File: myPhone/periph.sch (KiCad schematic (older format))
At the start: 57 parts, among them J201 ESP32.UART, J202 Modem, J203 SIM_Card, J204 Motor, J205 Micro_SD_Card, J206 Camera, J207 GPS, SW201 BOOT, U201 ESP32-WROOM, U202 SN74CBTLV3125, U203 TXB0104RGY, U204 TXB0104RGY, U205 DRV2605L, U206 SN74CBTLV3126, U207 TPS22917, U208 SN74LVC2G66, U209 TPS22917

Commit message: upgrade to kicad 5; fixed footprints
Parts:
- removed J201: ESP32.UART, Pin_Headers:Pin_Header_Straight_1x03_Pitch2.54mm, symbol Conn_01x03
- removed J202: Modem, footprints:mpcie-socket, symbol Conn_02x26_Odd_Even
- removed J203: SIM_Card, footprints:Wurth_NanoSIM-693043020611, symbol SIM_Card
- removed J204: Motor, Pin_Headers:Pin_Header_Straight_1x02_Pitch1.27mm, symbol Conn_01x02
- removed J205: Micro_SD_Card, footprints:MicroSd, symbol Micro_SD_Card
- removed J206: Camera, Pin_Headers:Pin_Header_Straight_1x08_Pitch2.54mm, symbol Conn_01x08
- removed J207: GPS, Pin_Headers:Pin_Header_Straight_1x04_Pitch2.54mm, symbol Conn_01x04
- removed JP202: UART SW, Pin_Headers:Pin_Header_Straight_2x04_Pitch1.27mm, symbol Conn_02x04_Odd_Even
- removed SW201: BOOT, footprints:Panasonic_EVPBB, symbol SW_Push
- removed U203, U204: TXB0104RGY, footprints:Texas_S-PVQFN-N14_ThermalVias, symbol TXB0104RGY
- added J201: ESP32.UART, Connector_PinHeader_2.54mm:PinHeader_1x03_P2.54mm_Vertical, symbol Connector_Generic:Conn_01x03
- added J202: Modem, footprints:mpcie-socket, symbol Connector_Generic:Conn_02x26_Odd_Even
- added J203: SIM_Card, footprints:Wurth_NanoSIM-693043020611, symbol Connector:SIM_Card
- added J204: Motor, Connector_PinHeader_1.27mm:PinHeader_1x02_P1.27mm_Vertical, symbol Connector_Generic:Conn_01x02
- added J205: Micro_SD_Card, footprints:MicroSd, symbol Connector:Micro_SD_Card
- added J206: Camera, Connector_PinHeader_2.54mm:PinHeader_1x08_P2.54mm_Vertical, symbol Connector_Generic:Conn_01x08
- added J207: GPS, Connector_PinHeader_2.54mm:PinHeader_1x04_P2.54mm_Vertical, symbol Connector_Generic:Conn_01x04
- added JP202: UART SW, Connector_PinHeader_1.27mm:PinHeader_2x04_P1.27mm_Vertical, symbol Connector_Generic:Conn_02x04_Odd_Even
- added SW201: BOOT, footprints:Panasonic_EVPBB, symbol Switch:SW_Push
- added U203, U204: TXB0104RGY, Package_DFN_QFN:Texas_S-PVQFN-N14_ThermalVias, symbol Logic_LevelTranslator:TXB0104RGY
- C201, C202, C203, C204, C205, C206, C207, C208, C210, C211, C212, C213, C214, C215, C216, C217, C218, C219, C220, C221, C222, C223, C224, C225, C226: footprint Capacitors_SMD:C_0603 -> Capacitor_SMD:C_0603_1608Metric; symbol C -> Device:C
- C209: footprint Capacitors_Tantalum_SMD:CP_Tantalum_Case-B_EIA-3528-21_Reflow -> Capacitor_Tantalum_SMD:CP_EIA-3528-21_Kemet-B; symbol CP -> Device:CP
- JP201: footprint Pin_Headers:Pin_Header_Straight_1x02_Pitch1.27mm -> Connector_PinHeader_1.27mm:PinHeader_1x02_P1.27mm_Vertical; symbol Jumper_NC_Small -> Device:Jumper_NC_Small
- JP203: footprint Pin_Headers:Pin_Header_Straight_1x03_Pitch1.27mm -> Connector_PinHeader_1.27mm:PinHeader_1x03_P1.27mm_Vertical; symbol Jumper_NC_Dual -> Device:Jumper_NC_Dual
- R201, R202, R203, R204, R205, R206, R207, R208, R209, R210, R211: footprint Resistors_SMD:R_0603 -> Resistor_SMD:R_0603_1608Metric; symbol R -> Device:R
- U201: symbol ESP32-WROOM -> esp32:ESP32-WROOM
- U202: footprint footprints:Texas_S-PVQFN-N14_ThermalVias -> Package_DFN_QFN:Texas_S-PVQFN-N14_ThermalVias; symbol SN74CBTLV3125 -> sn74:SN74CBTLV3125
- U205: footprint footprints:VSSOP-10_3x3mm_Pitch0.5mm -> Package_SO:VSSOP-10_3x3mm_P0.5mm; symbol DRV2605L -> drv2605l:DRV2605L
- U206: footprint footprints:Texas_S-PVQFN-N14_ThermalVias -> Package_DFN_QFN:Texas_S-PVQFN-N14_ThermalVias; symbol SN74CBTLV3126 -> sn74:SN74CBTLV3126
- U207, U209: symbol TPS22917 -> texas-tps:TPS22917
- U208: footprint Housings_SSOP:VSSOP-8_2.3x2mm_Pitch0.5mm -> Package_SO:VSSOP-8_2.4x2.1mm_P0.5mm; symbol SN74LVC2G66 -> sn74:SN74LVC2G66
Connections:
- net +1V8: now also U203.1 (VCCA), U203.8 (OE), U204.1 (VCCA)
- net +3V3: now also J202.2 (Pin_2), J202.24 (Pin_24), J202.39 (Pin_39), J202.41 (Pin_41), J202.52 (Pin_52), J205.4 (VDD), U203.14 (VCCB), U204.14 (VCCB)
- net CAM.MISO: now also J206.3 (Pin_3)
- net CAM.MOSI: now also J206.2 (Pin_2)
- net CAM.PWR: now also J206.6 (Pin_6)
- net CAM.SCK: now also J206.4 (Pin_4)
- net CAM.SCL: now also J206.8 (Pin_8)
- net CAM.SDA: now also J206.7 (Pin_7)
- net ESP32.PCM.CLK: now also U203.13 (B1)
- net ESP32.PCM.DI: now also U203.12 (B2)
- net ESP32.PCM.DO: now also U203.11 (B3)
- net ESP32.PCM.SYNC: now also SW201.1, U203.10 (B4)
- net ESP32.U2.DTR: now also JP202.1 (Pin_1), U204.13 (B1)
- net ESP32.U2.RI: now also JP202.3 (Pin_3), U204.12 (B2)
- net ESP32.U2.RXD: now also JP202.5 (Pin_5), U204.11 (B3)
- net ESP32.U2.TXD: now also JP202.7 (Pin_7), U204.10 (B4)
- net GND: now also J201.3 (Pin_3), J202.15 (Pin_15), J202.18 (Pin_18), J202.21 (Pin_21), J202.26 (Pin_26), J202.27 (Pin_27), J202.29 (Pin_29), J202.34 (Pin_34), J202.35 (Pin_35), J202.37 (Pin_37), J202.4 (Pin_4), J202.40 (Pin_40), J202.43 (Pin_43), J202.50 (Pin_50), J202.9 (Pin_9), J203.5 (GND), J205.6 (VSS), J206.5 (Pin_5), J207.4 (Pin_4), SW201.2, U203.15 (Pad), U203.7 (GND), U204.15 (Pad), U204.7 (GND)
- net GPIO_23: now also J206.1 (Pin_1)
- net Modem.PCM.CLK: now also J202.45 (Pin_45), U203.2 (A1)
- net Modem.PCM.DI: now also J202.49 (Pin_49), U203.4 (A3)
- net Modem.PCM.DO: now also J202.47 (Pin_47), U203.3 (A2)
- net Modem.PCM.SYNC: now also J202.51 (Pin_51), U203.5 (A4)
- net Quectel.UART.DTR: now also J202.31 (Pin_31), JP202.2 (Pin_2)
- net Quectel.UART.RI: now also J202.17 (Pin_17), JP202.4 (Pin_4), U204.5 (A4)
- net Quectel.UART.RXD: now also J202.11 (Pin_11), JP202.8 (Pin_8)
- net Quectel.UART.TXD: now also J202.13 (Pin_13), JP202.6 (Pin_6)
- net SIMCom.UART.DTR: now also J202.46 (Pin_46), U204.2 (A1)
- net SIMCom.UART.RI: now also J202.44 (Pin_44), U204.3 (A2)
- net SIMCom.UART.TXD: now also J202.19 (Pin_19), U204.4 (A3)
- net SPI1.MISO: now also J205.7 (DAT0)
- net SPI1.MOSI: now also J205.2 (DAT3/CD)
- net SPI1.SCK: now also J205.5 (CLK)
- net SPI1.SS0: now also J205.1 (DAT2)
- net UART0.RX: now also J207.3 (Pin_3)
- net UART0.TX: now also J207.2 (Pin_2)
- net at U201.34 (RXD0): now also J201.2 (Pin_2)
- net at U201.35 (TXD0): now also J201.1 (Pin_1)
- net at R204.2: now also J202.10 (Pin_10)
- net at R205.2: now also J202.12 (Pin_12)
- net at R206.2: now also J202.14 (Pin_14)
- net at C204.1, C208.1, R203.2: now also J202.8 (Pin_8), J203.1 (VCC)
- net at C205.1, R206.1: now also J203.2 (RST)
- net at C206.1, R205.1: now also J203.3 (CLK)
- net at C207.1, JP201.2, R204.1: now also J203.7 (I/O)
- net at JP203.2: now also U204.8 (OE)
- net at U205.7 (OUT+): now also J204.1 (Pin_1)
- net at U205.9 (OUT-): now also J204.2 (Pin_2)
- net at U209.6 (VOUT): now also J207.1 (Pin_1)

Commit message: REV1 board
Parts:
- removed J201: ESP32.UART, Connector_PinHeader_2.54mm:PinHeader_1x03_P2.54mm_Vertical, symbol Connector_Generic:Conn_01x03
- removed J207: GPS, Connector_PinHeader_2.54mm:PinHeader_1x04_P2.54mm_Vertical, symbol Connector_Generic:Conn_01x04
- removed JP202: UART SW, Connector_PinHeader_1.27mm:PinHeader_2x04_P1.27mm_Vertical, symbol Connector_Generic:Conn_02x04_Odd_Even
- added C227: 470uF, Capacitor_Tantalum_SMD:CP_EIA-3528-21_Kemet-B, symbol Device:CP
- added JP203: Q.DTR, Connector_PinHeader_1.27mm:PinHeader_1x02_P1.27mm_Vertical, symbol Device:Jumper_NC_Small
- added JP204: Q.RI, Connector_PinHeader_1.27mm:PinHeader_1x02_P1.27mm_Vertical, symbol Device:Jumper_NC_Small
- added JP205: Q.TXD, Connector_PinHeader_1.27mm:PinHeader_1x02_P1.27mm_Vertical, symbol Device:Jumper_NC_Small
- added JP206: Q.RXD, Connector_PinHeader_1.27mm:PinHeader_1x02_P1.27mm_Vertical, symbol Device:Jumper_NC_Small
- R208: value 47K -> 100K
- renumbered C209 to C228, JP203 to JP202
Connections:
- net +3V3: now also C227.1; no longer R208.2, U202.13 (/4OE)
- net ESP32.I2C0.SCL: now also U201.10 (IO25); no longer U201.11 (IO26)
- net ESP32.I2C0.SDA: now also U201.11 (IO26); no longer U201.10 (IO25)
- net ESP32.PCM.SYNC: now also U201.26 (IO4); no longer SW201.1, U201.25 (IO0)
- net ESP32.U2.DTR: now also U204.12 (B2), JP203.1; no longer U204.13 (B1)
- net ESP32.U2.RI: now also U204.13 (B1), JP204.1; no longer U204.12 (B2)
- net ESP32.U2.RXD: now also U201.28 (IO17), JP205.1; no longer U201.27 (IO16)
- net ESP32.U2.TXD: now also U201.27 (IO16), JP206.1; no longer U201.28 (IO17)
- net FT813.GPIO0: now also R210.2, U206.1 (1OE), U206.10 (3OE), U206.4 (2OE), U207.3 (ON), U208.3 (2C), U208.7 (1C); no longer R211.1, U209.3 (ON)
- net FT813.GPIO1: now also R211.1, U209.3 (ON); no longer R210.2, U206.1 (1OE), U206.10 (3OE), U206.4 (2OE), U207.3 (ON), U208.3 (2C), U208.7 (1C)
- net FT813.GPIO3: now also R208.2; no longer R208.1
- net GND: now also R208.1, C227.2; no longer U202.11 (4B), U202.12 (4A)
- net Quectel.UART.DTR: now also JP203.2
- net Quectel.UART.RI: now also JP204.2
- net Quectel.UART.RXD: now also JP206.2
- net Quectel.UART.TXD: now also JP205.2
- net SIMCom.UART.DTR: now also U204.3 (A2); no longer U204.2 (A1)
- net SIMCom.UART.RI: now also U204.2 (A1); no longer U204.3 (A2)
- net SPI1.SCK: now also U202.11 (4B); no longer U201.30 (IO18)
- net SPI1.SS3: now also U202.13 (/4OE)
- net WAKE: now also U201.25 (IO0); no longer U201.26 (IO4)
- net at C203.1, R201.2, U201.3 (EN): now also SW201.1
- net ESP32.RXD0: now reaches U201.34 (RXD0)
- net ESP32.TXD0: now reaches U201.35 (TXD0)
- net TPS.VOUT: now reaches U209.6 (VOUT)
- net iMX8_USB1_D_N: now reaches J202.36 (Pin_36)
- net iMX8_USB1_D_P: now reaches J202.38 (Pin_38)
- new net ESP32.VSPI.SCK: U201.30 (IO18), U202.12 (4A)
- no-connect marks 31 -> 29
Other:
- moved on the sheet: C201, C202, C203, R201, R202, R208, SW201, U201

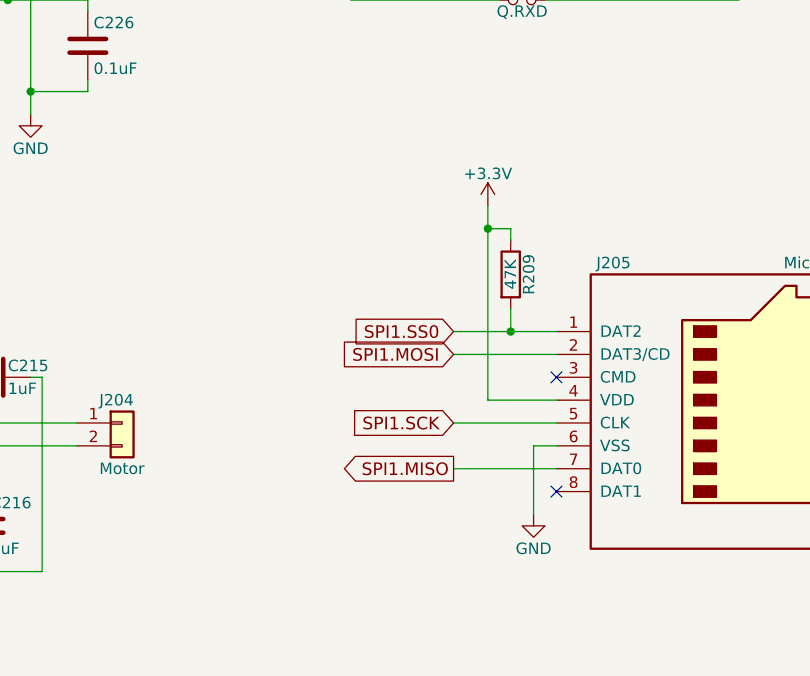
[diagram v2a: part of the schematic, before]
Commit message: display switch pull resistors added
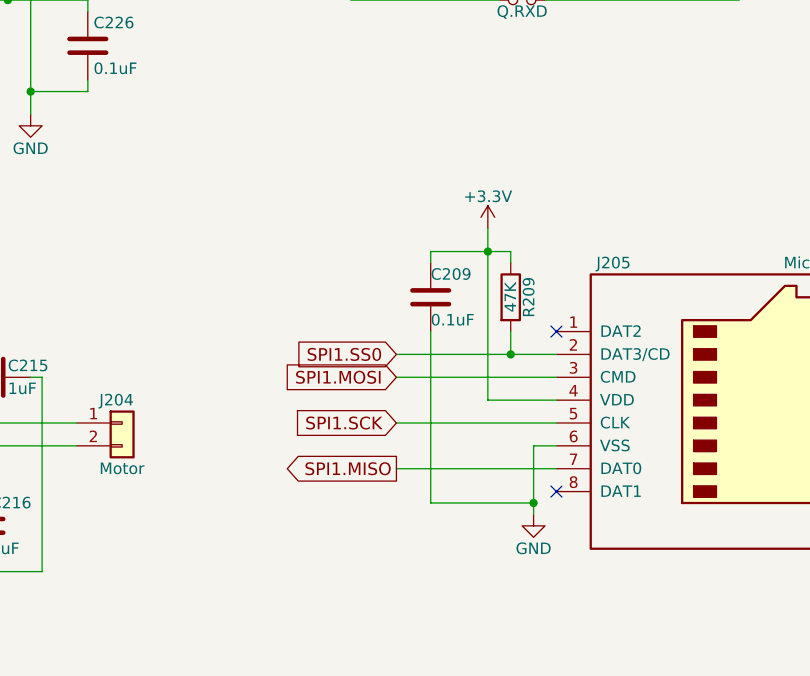
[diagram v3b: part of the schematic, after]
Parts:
- added C209: 0.1uF, Capacitor_SMD:C_0603_1608Metric, symbol Device:C
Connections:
- net +3V3: now also C209.1
- net GND: now also C209.2
- net SPI1.MOSI: now also J205.3 (CMD); no longer J205.2 (DAT3/CD)
- net SPI1.SS0: now also J205.2 (DAT3/CD); no longer J205.1 (DAT2)
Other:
- moved on the sheet: R209
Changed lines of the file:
@@
 Text GLabel 5700 5550 0    55   BiDi ~ 0
 FT813.GPIO3
-Text GLabel 9300 5550 0    55   Input ~ 0
+Text GLabel 9050 5550 0    55   Input ~ 0
 SPI1.SCK
-Text GLabel 9300 5750 0    55   Output ~ 0
+Text GLabel 9050 5750 0    55   Output ~ 0
 SPI1.MISO
-Text GLabel 9300 5250 0    55   Input ~ 0
-SPI1.MOSI
-Text GLabel 9300 5150 0    55   Input ~ 0
-SPI1.SS0
-$Comp
-L power:+3.3V #PWR098
-U 1 1 5C4FB85D
-P 9450 4600
-F 0 "#PWR098" H 9450 4450 50  0001 C CNN
-F 1 "+3.3V" H 9450 4740 50  0000 C CNN
-F 2 "" H 9450 4600 50  0001 C CNN
-F 3 "" H 9450 4600 50  0001 C CNN
-	1    9450 4600
-	-1   0    0    -1
-$EndComp
 $Comp
 L power:GND #PWR099
@@
 	1    0    0    -1
 $EndComp
-NoConn ~ 9750 5350
 NoConn ~ 9750 5850
 NoConn ~ 11450 6050
@@
 $EndComp
 $Comp
-L Device:R R209
-U 1 1 5C6D9747
-P 9550 4900
-F 0 "R209" V 9630 4900 50  0000 C CNN
-F 1 "47K" V 9550 4900 50  0000 C CNN
-F 2 "Resistor_SMD:R_0603_1608Metric" V 9480 4900 50  0001 C CNN
-F 3 "" H 9550 4900 50  0001 C CNN
-	1    9550 4900
-	1    0    0    -1
-$EndComp
-$Comp
 L power:+1V8 #PWR0112
 U 1 1 5C7053D3
@@
 $EndComp
 Wire Wire Line
-	9300 5150 9550 5150
-Wire Wire Line
-	9300 5250 9750 5250
-Wire Wire Line
-	9300 5550 9750 5550
-Wire Wire Line
-	9300 5750 9750 5750
-Wire Wire Line
-	9450 5450 9750 5450
-Wire Wire Line
-	9450 4600 9450 4700
+	9050 5750 9750 5750
 Wire Wire Line
 	9750 5650 9650 5650
 Wire Wire Line
-	9650 5650 9650 5950
+	9650 5650 9650 5900
 Wire Wire Line
 	1600 950  1600 1000
@@
 Wire Wire Line
 	4100 1450 4100 1500
-Wire Wire Line
-	9550 4750 9550 4700
-Wire Wire Line
-	9550 4700 9450 4700
-Connection ~ 9450 4700
-Wire Wire Line
-	9550 5050 9550 5150
-Connection ~ 9550 5150
 Wire Wire Line
 	13500 3150 13500 3300
@@
 	9800 1500 9900 1500
 Wire Wire Line
-	9450 4700 9450 5450
-Wire Wire Line
-	9550 5150 9750 5150
-Wire Wire Line
 	13700 3300 13700 3400
 Wire Wire Line
@@
 	6000 1300 6350 1300
 Connection ~ 6350 1300
+Wire Wire Line
+	9050 5550 9750 5550
+Wire Wire Line
+	9550 5250 9750 5250
+Connection ~ 9550 5250
+Wire Wire Line
+	9550 5150 9550 5250
+Wire Wire Line
+	9550 4800 9450 4800
+Wire Wire Line
+	9550 4850 9550 4800
+Wire Wire Line
+	9450 4700 9450 4800
+Wire Wire Line
+	9050 5350 9750 5350
+Wire Wire Line
+	9050 5250 9550 5250
+$Comp
+L Device:R R209
+U 1 1 5C6D9747
+P 9550 5000
+F 0 "R209" V 9630 5000 50  0000 C CNN
+F 1 "47K" V 9550 5000 50  0000 C CNN
+F 2 "Resistor_SMD:R_0603_1608Metric" V 9480 5000 50  0001 C CNN
+F 3 "" H 9550 5000 50  0001 C CNN
+	1    9550 5000
+	1    0    0    -1
+$EndComp
+$Comp
+L power:+3.3V #PWR098
+U 1 1 5C4FB85D
+P 9450 4700
+F 0 "#PWR098" H 9450 4550 50  0001 C CNN
+F 1 "+3.3V" H 9450 4840 50  0000 C CNN
+F 2 "" H 9450 4700 50  0001 C CNN
+F 3 "" H 9450 4700 50  0001 C CNN
+	1    9450 4700
+	-1   0    0    -1
+$EndComp
+Text GLabel 9050 5250 0    55   Input ~ 0
+SPI1.SS0
+Text GLabel 9050 5350 0    55   Input ~ 0
+SPI1.MOSI
+Wire Wire Line
+	9750 5450 9450 5450
+Wire Wire Line
+	9450 5450 9450 4800
+Connection ~ 9450 4800
+NoConn ~ 9750 5150
+$Comp
+L Device:C C209
+U 1 1 5D9958BB
+P 9200 5000
+F 0 "C209" H 9200 5100 50  0000 L CNN
+F 1 "0.1uF" H 9200 4900 50  0000 L CNN
+F 2 "Capacitor_SMD:C_0603_1608Metric" H 9238 4850 50  0001 C CNN
+F 3 "~" H 9200 5000 50  0001 C CNN
+	1    9200 5000
+	1    0    0    -1
+$EndComp
+Wire Wire Line
+	9200 5150 9200 5900
+Wire Wire Line
+	9200 5900 9650 5900
+Connection ~ 9650 5900
+Wire Wire Line
+	9650 5900 9650 5950
+Wire Wire Line
+	9200 4850 9200 4800
+Wire Wire Line
+	9200 4800 9450 4800
 $EndSCHEMATC

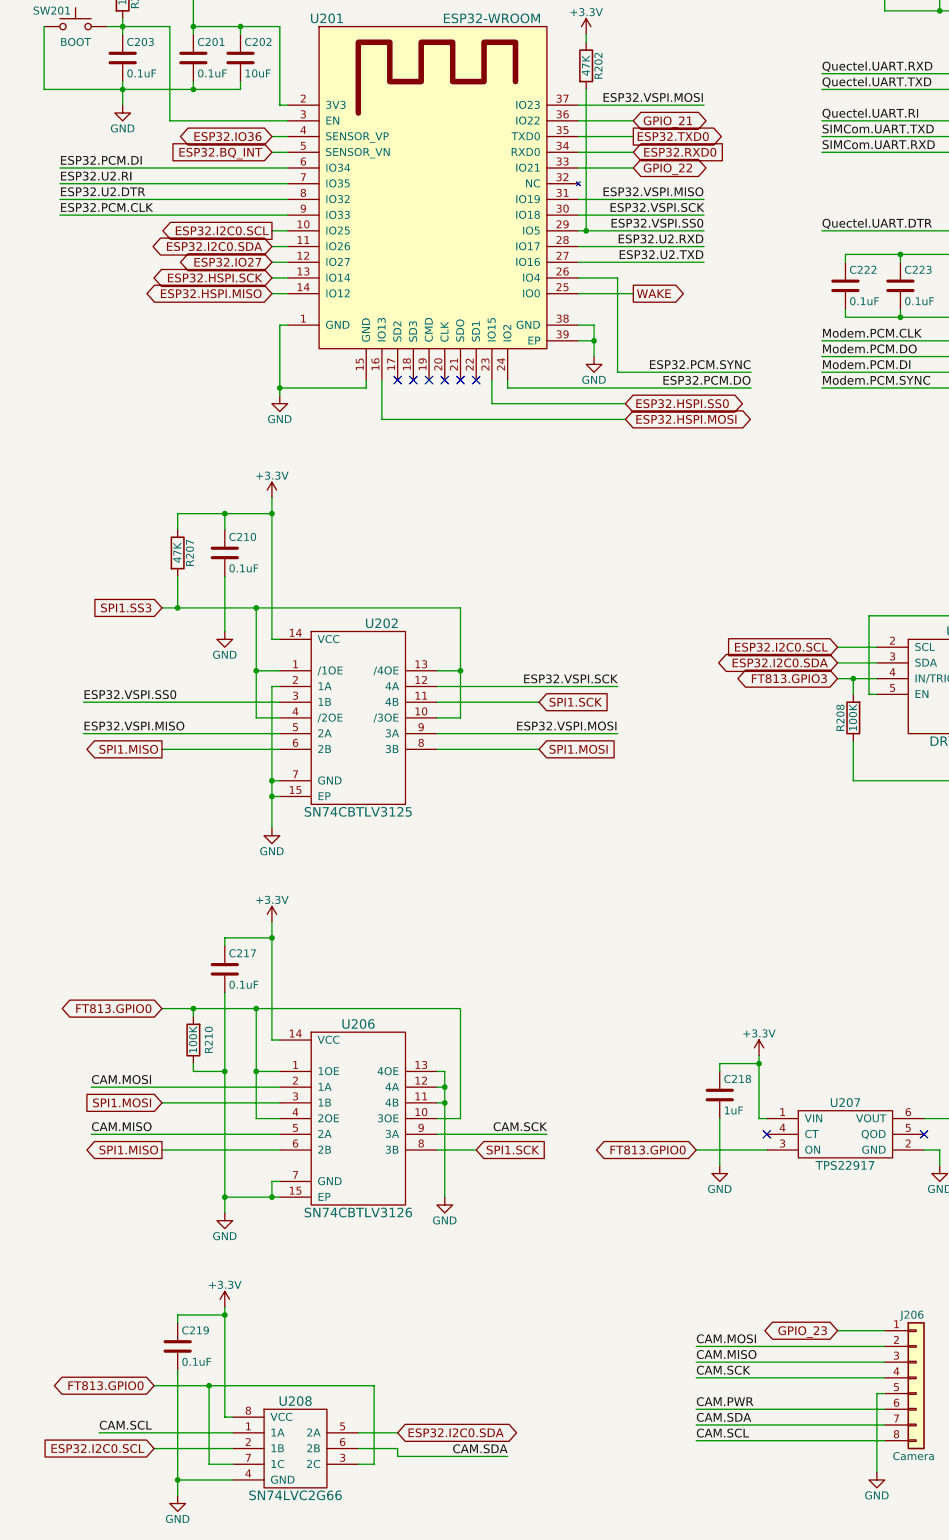
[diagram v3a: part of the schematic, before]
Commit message: fixed battery charger; added i2c switch for fe310; swapped pwm1/pwm2 for mic/spk
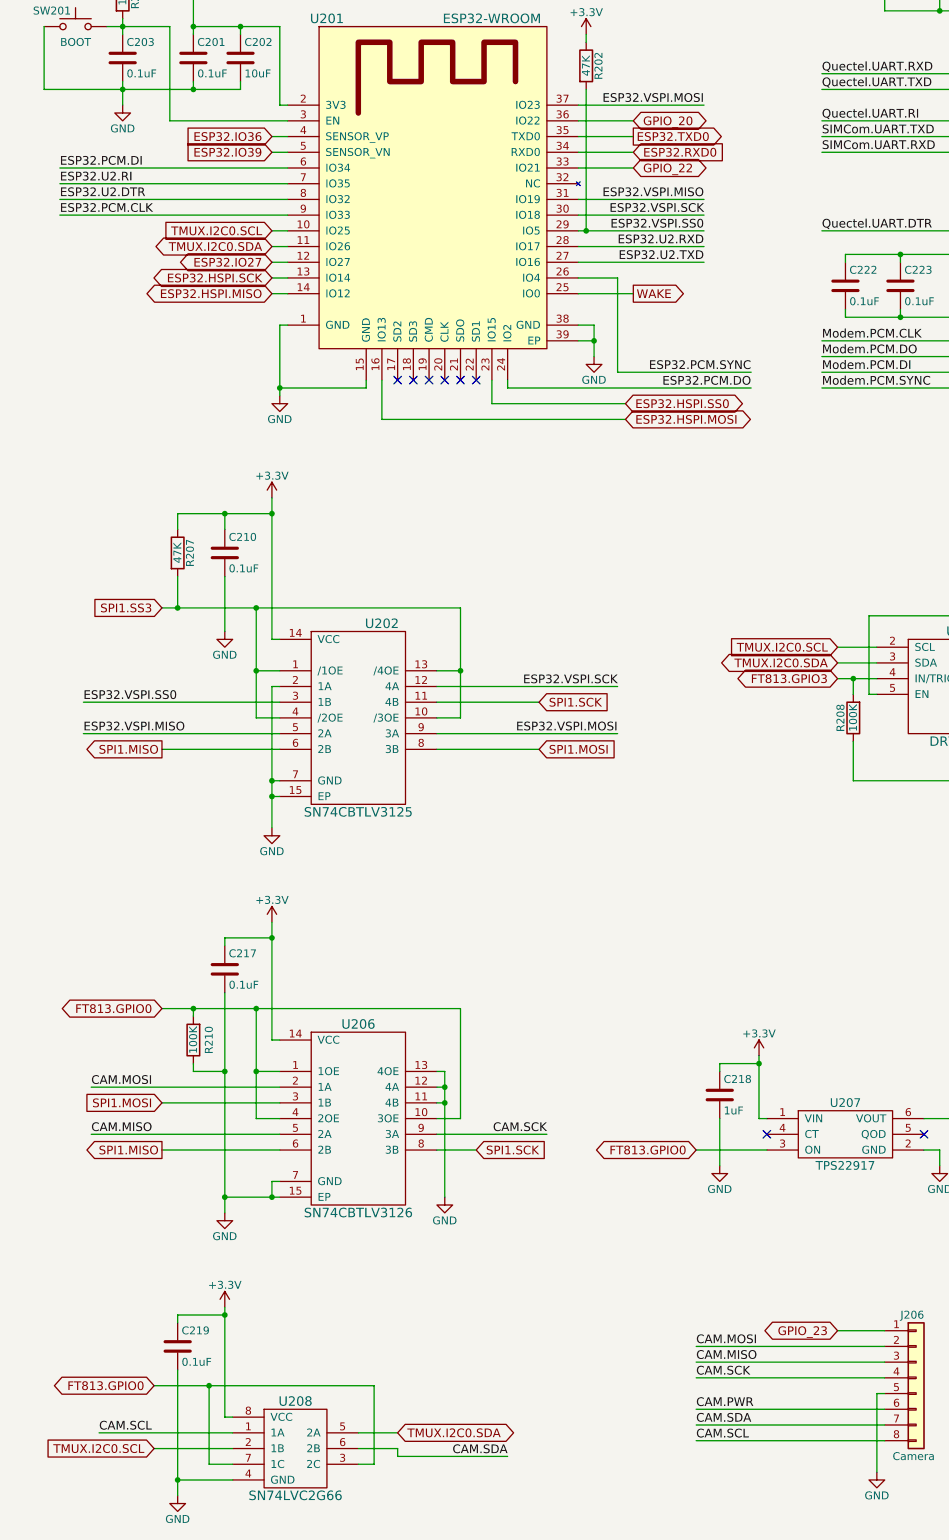
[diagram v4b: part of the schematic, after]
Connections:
- net ESP32.BQ_INT renamed ESP32.IO39
- net ESP32.I2C0.SCL renamed TMUX.I2C0.SCL
- net ESP32.I2C0.SDA renamed TMUX.I2C0.SDA
- net GPIO_21 renamed GPIO_20
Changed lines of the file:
@@
 SPI1.MOSI
 Text GLabel 4400 2000 2    55   BiDi ~ 0
-GPIO_21
+GPIO_20
 Text GLabel 4400 2300 2    55   BiDi ~ 0
 GPIO_22
@@
 	1    0    0    -1
 $EndComp
-Text GLabel 2100 2700 0    55   Output ~ 0
-ESP32.I2C0.SCL
+Text GLabel 2100 2700 0    55   Input ~ 0
+TMUX.I2C0.SCL
 Text GLabel 2100 2800 0    55   BiDi ~ 0
-ESP32.I2C0.SDA
+TMUX.I2C0.SDA
 Text GLabel 4400 3100 2    55   Output ~ 0
 WAKE
@@
 $EndComp
 Text GLabel 2100 2200 0    55   Input ~ 0
-ESP32.BQ_INT
+ESP32.IO39
 $Comp
 L Device:Jumper_NC_Dual JP202
@@
 	5900 5150 7100 5150
 Text GLabel 5700 5350 0    55   Input ~ 0
-ESP32.I2C0.SCL
+TMUX.I2C0.SCL
 Text GLabel 5700 5450 0    55   BiDi ~ 0
-ESP32.I2C0.SDA
+TMUX.I2C0.SDA
 Wire Wire Line
 	5700 5350 5950 5350
@@
 FT813.GPIO0
 Text GLabel 2900 10350 2    55   BiDi ~ 0
-ESP32.I2C0.SDA
+TMUX.I2C0.SDA
 Text GLabel 1350 10450 0    55   Input ~ 0
-ESP32.I2C0.SCL
+TMUX.I2C0.SCL
 Text GLabel 3400 8550 2    55   Input ~ 0
 SPI1.SCK
@@
 Wire Wire Line
 	2100 2900 2200 2900
-Text GLabel 2100 2100 0    55   BiDi ~ 0
+Text GLabel 2100 2100 0    55   Input ~ 0
 ESP32.IO36
 Wire Wire Line
